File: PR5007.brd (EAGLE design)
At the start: 70 x 70 mm, 47 parts

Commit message: smallish changes
tore up a few wires, changed ground plane somehow
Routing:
- net N$21: track 38.4 -> 7.62 mm
- net N$14: track 17.2 -> 7.62 mm
- net N$22: track 25.7 -> 26.6 mm
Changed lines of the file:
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@@
 <?xml version="1.0" encoding="utf-8"?>
 <!DOCTYPE eagle SYSTEM "eagle.dtd">
-<eagle version="6.4">
+<eagle version="6.6.0">
 <drawing>
 <settings>
@@
 <setting verticaltext="up"/>
 </settings>
-<grid distance="1" unitdist="mil" unit="mil" style="lines" multiple="1" display="yes" altdistance="0.1" altunitdist="mm" altunit="mm"/>
+<grid distance="1" unitdist="mil" unit="mm" style="lines" multiple="1" display="yes" altdistance="0.1" altunitdist="mm" altunit="mm"/>
 <layers>
 <layer number="1" name="Top" color="4" fill="1" visible="yes" active="yes"/>
@@
 <polygon width="0.4064" layer="16" isolate="0.3048">
 <vertex x="35" y="70" curve="-90"/>
-<vertex x="70" y="35" curve="-100"/>
+<vertex x="70" y="35" curve="-90"/>
 <vertex x="35" y="0" curve="-90"/>
 <vertex x="0" y="35" curve="-90"/>
@@
 <wire x1="30.045" y1="59.055" x2="29.3" y2="59.8" width="0.3048" layer="1"/>
 <wire x1="29.3" y1="59.8" x2="29.3" y2="62.3" width="0.3048" layer="1"/>
-<wire x1="29.3" y1="62.3" x2="27.3" y2="64.3" width="0.3048" layer="1"/>
-<wire x1="27.3" y1="64.3" x2="27.09" y2="64.3" width="0.3048" layer="1"/>
-<wire x1="27.09" y1="64.3" x2="24.17" y2="64.3" width="0.3048" layer="1"/>
-<wire x1="24.17" y1="64.3" x2="24.14" y2="64.27" width="0.3048" layer="1"/>
 <wire x1="19" y1="62.2" x2="19" y2="57.995" width="0.3048" layer="1"/>
 <wire x1="19" y1="57.995" x2="19.26" y2="57.735" width="0.3048" layer="1"/>
@@
 <wire x1="19" y1="62.2" x2="19.8" y2="63" width="0.3048" layer="1"/>
 <wire x1="19.8" y1="63" x2="20.7" y2="63" width="0.3048" layer="1"/>
-<wire x1="20.7" y1="63" x2="22.05" y2="64.35" width="0.3048" layer="1"/>
-<wire x1="22.05" y1="64.35" x2="24.06" y2="64.35" width="0.3048" layer="1"/>
-<wire x1="24.06" y1="64.35" x2="24.14" y2="64.27" width="0.3048" layer="1"/>
-<wire x1="27.18" y1="64.39" x2="27.09" y2="64.3" width="0.3048" layer="1"/>
 <contactref element="C1" pad="+"/>
-<wire x1="27.18" y1="64.39" x2="27.18" y2="65.314" width="0.3048" layer="1"/>
+<wire x1="20.7" y1="63" x2="21.97" y2="64.27" width="0.3048" layer="1"/>
+<wire x1="21.97" y1="64.27" x2="24.14" y2="64.27" width="0.3048" layer="1"/>
+<wire x1="29.3" y1="62.3" x2="27.18" y2="64.42" width="0.3048" layer="1"/>
+<wire x1="27.18" y1="64.42" x2="27.18" y2="65.314" width="0.3048" layer="1"/>
+<wire x1="24.14" y1="64.27" x2="27.18" y2="64.27" width="0.3048" layer="1"/>
+<wire x1="27.18" y1="64.27" x2="27.18" y2="65.314" width="0.3048" layer="1"/>
 </signal>
 <signal name="N$31">
@@
 <contactref element="U$2" pad="POS"/>
 <contactref element="U$2" pad="POS@2"/>
-<wire x1="4.7244" y1="24.1476" x2="4.7244" y2="22.8916" width="1.016" layer="1"/>
-<wire x1="4.7244" y1="22.8916" x2="10.616" y2="17" width="1.016" layer="1"/>
 <wire x1="10.616" y1="17" x2="18.236" y2="17" width="1.016" layer="1"/>
+<wire x1="10.616" y1="17" x2="4.7244" y2="24.1476" width="0" layer="19" extent="1-1"/>
 </signal>
 <signal name="N$21">
@@
 <contactref element="U$1" pad="NEG"/>
 <wire x1="18.236" y1="53" x2="10.616" y2="53" width="1.016" layer="1"/>
-<wire x1="10.616" y1="53" x2="4.318" y2="48.5394" width="1.016" layer="1" curve="70.616576"/>
-<wire x1="4.318" y1="48.5394" x2="3.2258" y2="45.5422" width="1.016" layer="1" curve="-1.2773"/>
-<wire x1="3.2258" y1="45.5422" x2="2.0828" y2="41.3766" width="1.016" layer="1" curve="10.633933"/>
-<wire x1="2.0828" y1="41.3766" x2="1.4732" y2="36.1696" width="1.016" layer="1" curve="6.698784"/>
-<wire x1="1.4732" y1="36.1696" x2="1.9558" y2="30.0736" width="1.016" layer="1" curve="15.70897"/>
-<wire x1="1.9558" y1="30.0736" x2="3.7744" y2="26.2476" width="1.016" layer="1" curve="26.084061"/>
+<wire x1="3.7744" y1="26.2476" x2="10.616" y2="53" width="0" layer="19" extent="1-1"/>
 </signal>
 <signal name="N$30">

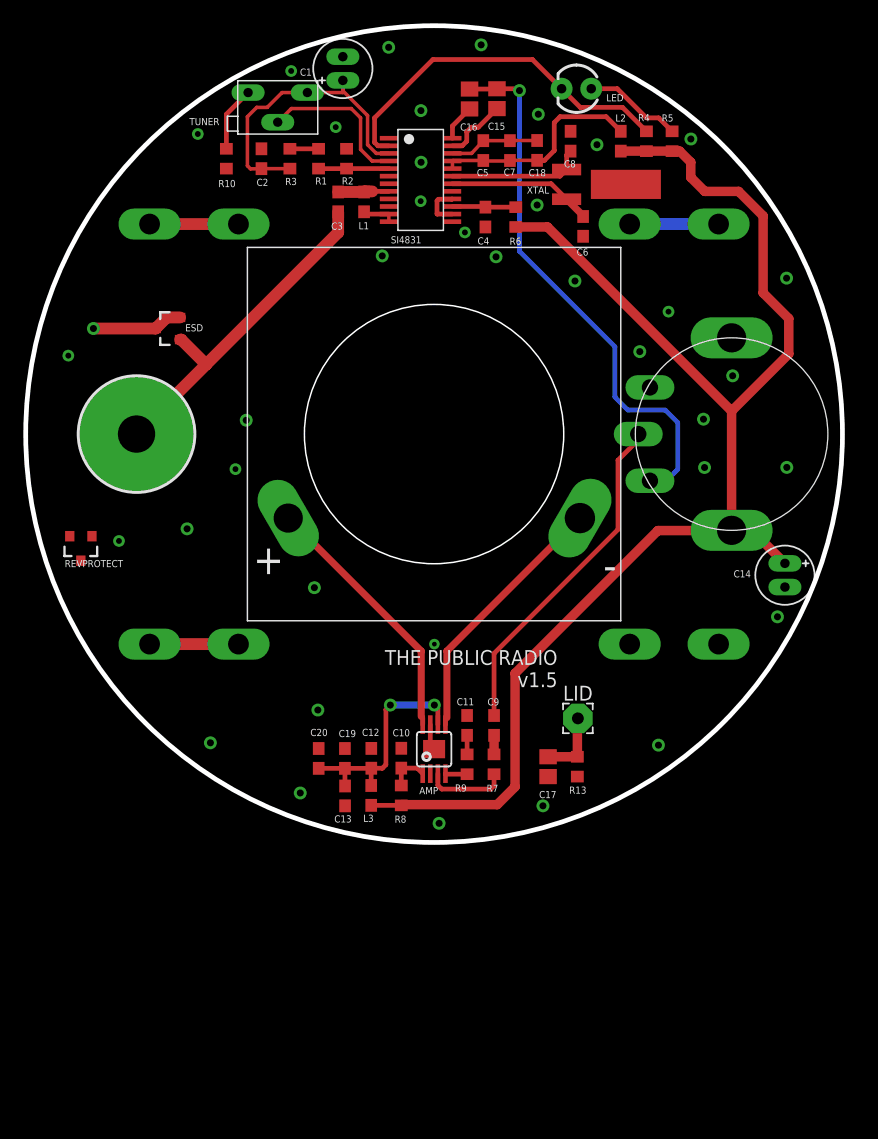
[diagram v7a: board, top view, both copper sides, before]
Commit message: bigger redesign
updated si4831 package; updated pot package; moved a bunch of stuff
around
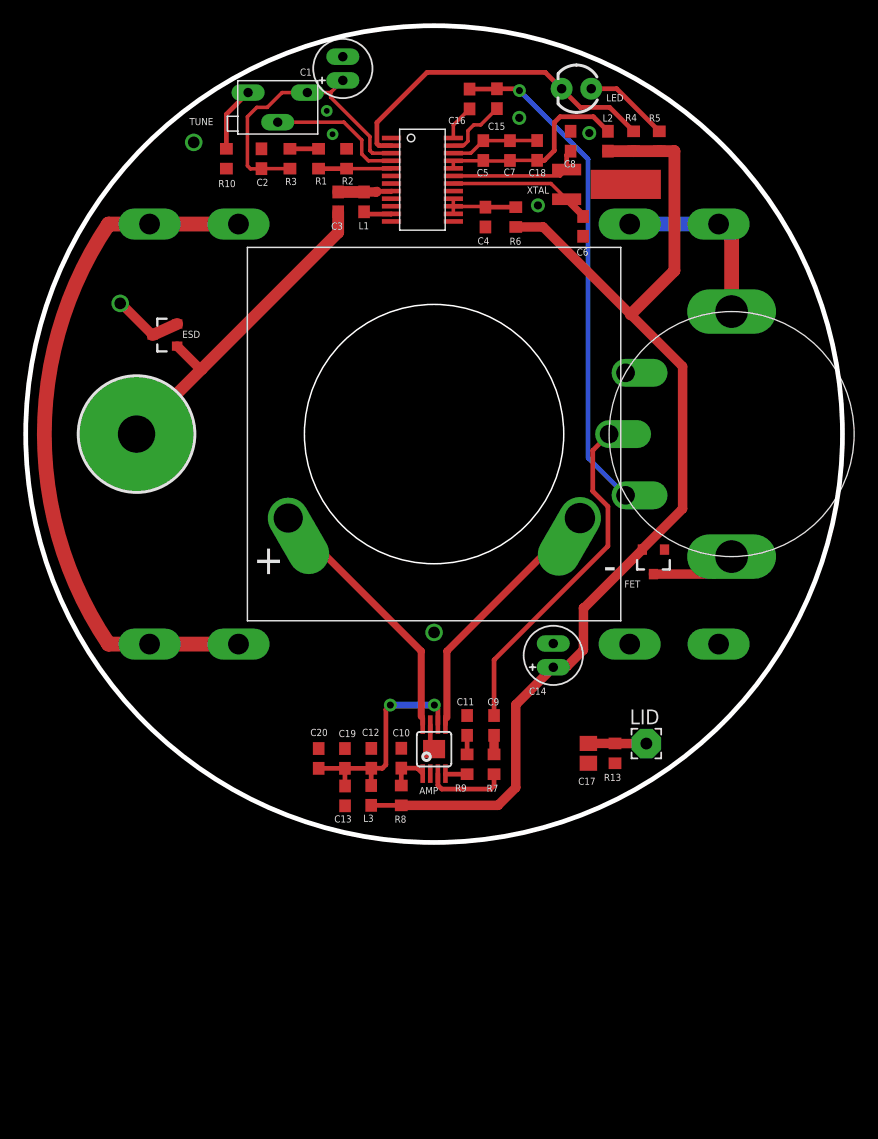
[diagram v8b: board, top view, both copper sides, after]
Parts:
- removed REVPROTECT: SI2333DDS, PubRadioLib:SI2333DDS
- removed SI4831: (no value), PublicRadioICs:SI4831-SSOP-24
- added FET: SI2333DDS, PubRadioLib:SI2333DDS
- added U$4: SI4831_FM_IC, PR_Libraries:SI4831_FM_IC
- C15, C16: value (none) -> 2.2uF; device resistor:C0805 -> resistor:C0603
- L2, L3: value (none) -> 2.5 kOhm @ 100MHz
- U$5: value P170_BOURNS_POT_SW -> RV170SF_TAIWANA_POT_SW; device PR_Libraries:P170_BOURNS_POT_SW -> PR_Libraries:RV170SF_TAIWANA_POT_SW
- moved C14 21.0 mm to (45.2, 16.0), turned to 90 degrees
- moved LID 6.25 mm to (53.2, 8.48)
- moved C17 3.64 mm to (48.2, 7.64)
- moved R13 3.42 mm to (50.5, 7.64)
- moved L2 1.10 mm to (49.9, 60.1)
- moved R4 1.10 mm to (52.1, 60.1)
- moved R5 1.10 mm to (54.3, 60.1)
- moved ESD 0.61 mm to (12.0, 43.5)
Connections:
- net GND: now also FET.1, U$4.AMI, U$4.GND, U$4.GND@2, U$4.NC@3, U$4.NC@4, U$4.RFGND, U$4.VOL+/TREBLE, U$4.VOL-/BASS; no longer REVPROTECT.1, SI4831.10, SI4831.11, SI4831.12, SI4831.13, SI4831.14, SI4831.16, SI4831.17, SI4831.9
- net N$10: now also U$4.XTALO; no longer SI4831.18
- net N$12: now also U$4.TUNE2; no longer SI4831.4
- net N$13: now also U$4.BAND; no longer SI4831.5
- net N$14: now also U$1.NEG, U$1.NEG@2; no longer REVPROTECT.3
- net N$15: now also U$4.FMI; no longer SI4831.8
- net N$16: now also U$4.VDD1, U$4.VDD2; no longer SI4831.20, SI4831.21
- net N$21: now also U$1.POS, U$1.POS@2, U$5.SW_OUT; no longer REVPROTECT.2, U$1.NEG, U$1.NEG@2
- net N$22: now also U$4.TUNE1; no longer SI4831.3
- net N$30: now also FET.3, U$5.SW_IN; no longer U$1.POS, U$1.POS@2
- net N$31: now also U$4.ROUT; no longer SI4831.23
- net N$33: now also U$4.LOUT; no longer SI4831.24
- net N$6: now also U$4.DBYP; no longer SI4831.22
- net N$7: now also U$4.XTALI; no longer SI4831.19
- net N$8: now also U$4.RST; no longer SI4831.15
- net N$9: now also U$4.STATION; no longer SI4831.2
- net VCC: now also FET.2; no longer U$5.SW_IN
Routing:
- net N$14: track 7.62 -> 58.3 mm
- net VCC: track 122.5 -> 96.2 mm
- net N$21: track 7.62 -> 15.6 mm
- net GND: track 16.7 -> 12.2 mm, vias 38 -> 8
- net N$5: track 47.1 -> 42.8 mm
- net N$9: track 31.4 -> 29.0 mm
- net N$12: track 13.5 -> 11.8 mm
- net N$16: track 18.8 -> 17.6 mm
- net N$11: track 8.44 -> 7.34 mm
- net N$34: track 5.82 -> 4.97 mm
- net N$22: track 26.6 -> 25.7 mm
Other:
- board text added: "BRD#"
- board text added: "FRQ"
- board text added: "TUNE"
- board text removed: "Board"
- board text removed: "Board #"
- board text removed: "Station"
- board text removed: "THE PUBLIC RADIO v1.5"
- board text removed: "TUNER"
